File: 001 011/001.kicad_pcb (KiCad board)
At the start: 2 copper layers, 25.3 x 22 mm, 8 parts, among them J1 USB_C_Receptacle_USB2.0, J2 Conn_01x14, J3 Conn_01x12

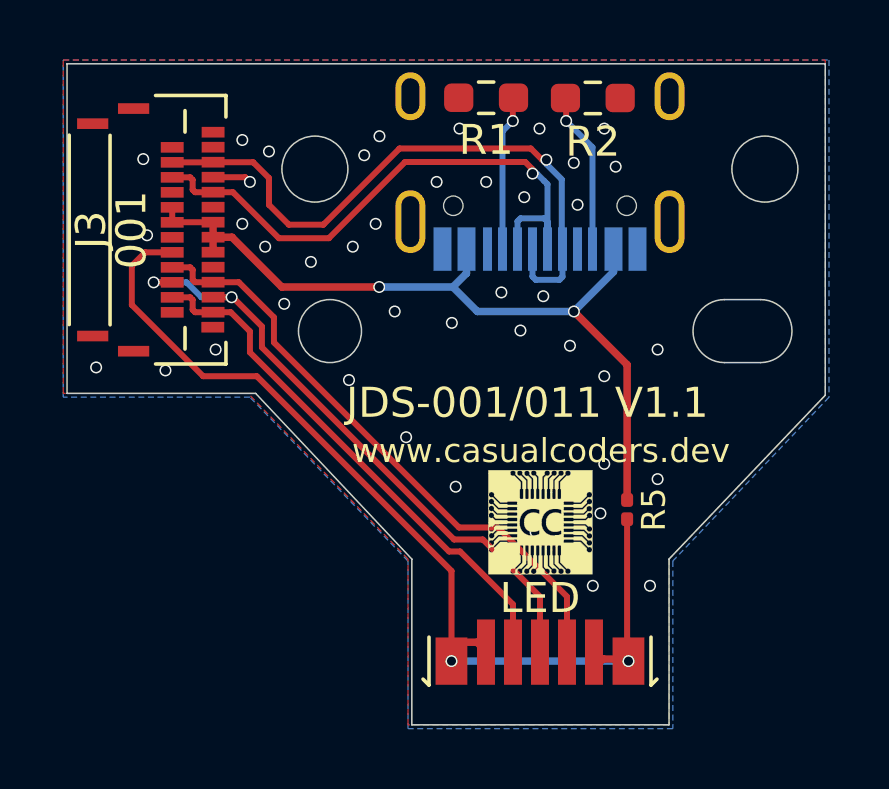
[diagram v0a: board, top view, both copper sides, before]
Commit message: 001, 011, 030 standardized to a cheaper LED
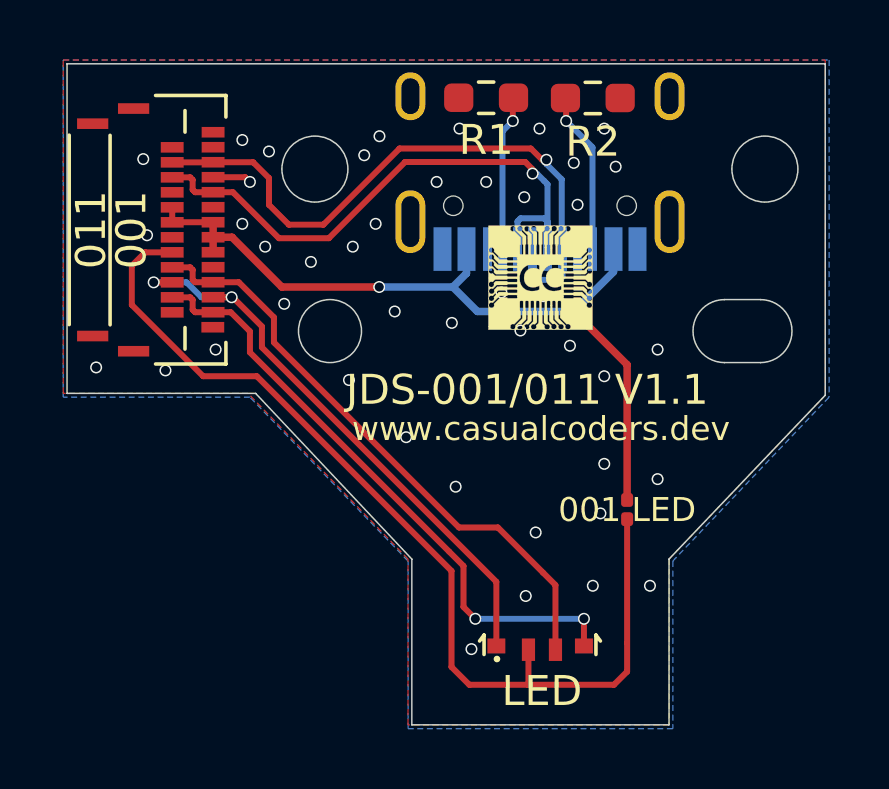
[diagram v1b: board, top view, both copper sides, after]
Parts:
- removed D1: MSL0104RGB, MSL0104RGB:MSL0104RGB
- removed R5: Bridge for 001, Resistor_SMD:R_0201_0603Metric
- added 001 LED: Bridge for 001, Resistor_SMD:R_0201_0603Metric, F.Cu at (122.8, 68.2)
- added LED: LED_RAGB, New_LED:FM-3510RGBA-SG, F.Cu at (120.0, 72.8)
- moved G*** 8.15 mm to (119.9, 60.5)
- renumbered J3 to 011, J1 to USB
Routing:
- net /B: track 17.2 -> 20.5 mm, vias 0 -> 2
- net /R: track 20.2 -> 19.3 mm
- net /Annode: track 32.4 -> 33.0 mm, vias 2 -> 0
- net GND: vias 42 -> 44
